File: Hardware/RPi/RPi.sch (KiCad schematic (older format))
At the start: 90 parts, among them P1 USB_B, P10 Solder_Pad, P11 Solder_Pad, P12 Solder_Pad, P13 Solder_Pad, P14 Solder_Pad, P15 Solder_Pad, P16 Solder_Pad, P17 Solder_Pad, P18 Solder_Pad, P19 Solder_Pad, P2 CONN_01X06, P3 USB_A, P4 USB_A, P5 USB_A, P6 USB_A, P7 Solder_Pad, P8 Solder_Pad, P9 Solder_Pad, U1 MPU_9150, U10 WS2812B, U11 WS2812B, U12 WS2812B, U13 Teensy_LC, U14 WS2812B, U15 WS2812B, U16 WS2812B, U17 WS2812B, U18 WS2812B, U19 WS2812B, U2 RPi_Interface, U3 FE1.1s, U4 AP1117E25, U5 Dual_buffer_NC7WZ16, U6 ESP-12E, U7 WS2812B, U8 WS2812B, U9 WS2812B, Y1 Crystal 12MHz

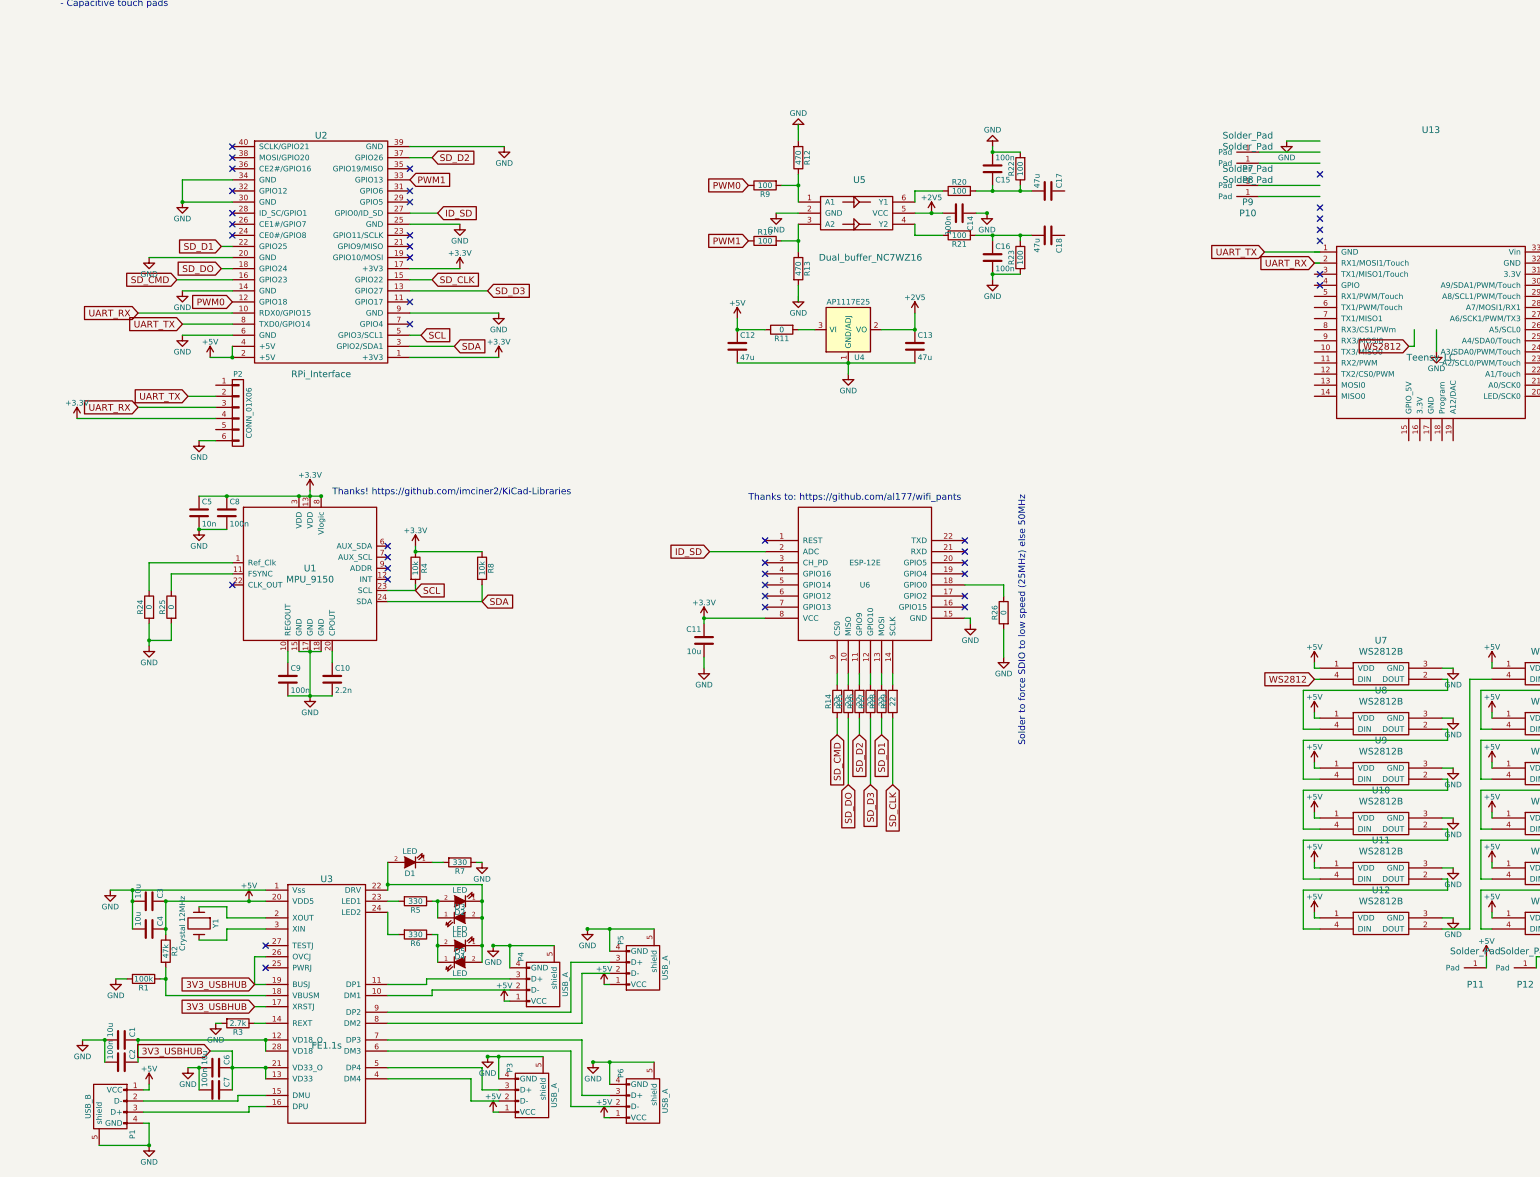
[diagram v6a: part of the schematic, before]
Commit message: Fixed schematic/component errors
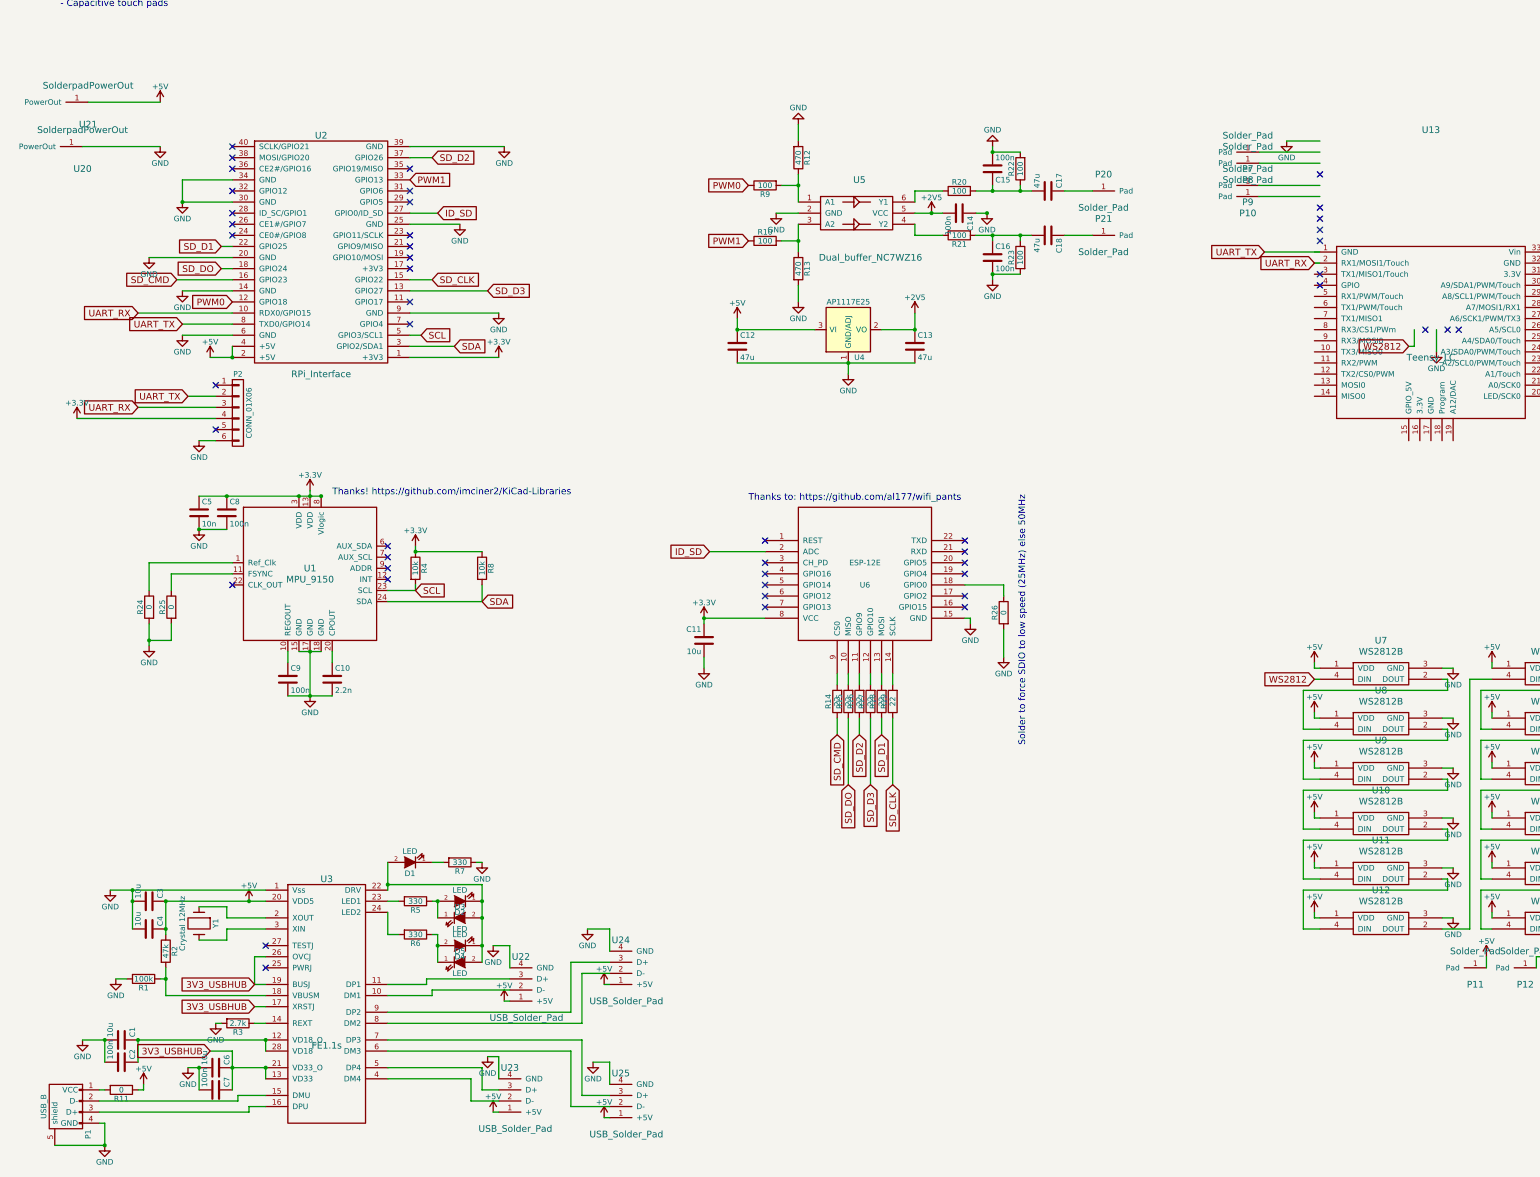
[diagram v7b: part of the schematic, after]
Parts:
- removed P3, P4, P5, P6: USB_A, TimeArc:USB_A_SMD_Pads, symbol USB_A
- added P20, P21: Solder_Pad, Measurement_Points:Measurement_Point_Square-SMD-Pad_Big, symbol Solder_Pad
- added U20, U21: SolderpadPowerOut, Measurement_Points:Measurement_Point_Square-SMD-Pad_Big, symbol SolderpadPowerOut
- added U22, U23, U24, U25: USB_Solder_Pad, TimeArc:USB_A_SMD_Pads, symbol USB_Solder_Pad
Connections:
- wire segments 315 -> 318
- no-connect marks 47 -> 53
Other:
- moved on the sheet: P1
